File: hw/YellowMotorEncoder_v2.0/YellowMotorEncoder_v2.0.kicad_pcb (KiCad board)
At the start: 2 copper layers, 22.8 x 20.3 mm, 30 parts, among them J1 Conn_01x06, Q1 AO3401A, U1 47k, U10 10k, U11 47k, U12 18p/50V, U13 BLUE, U14 10k, U15 BLUE, U16 10k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

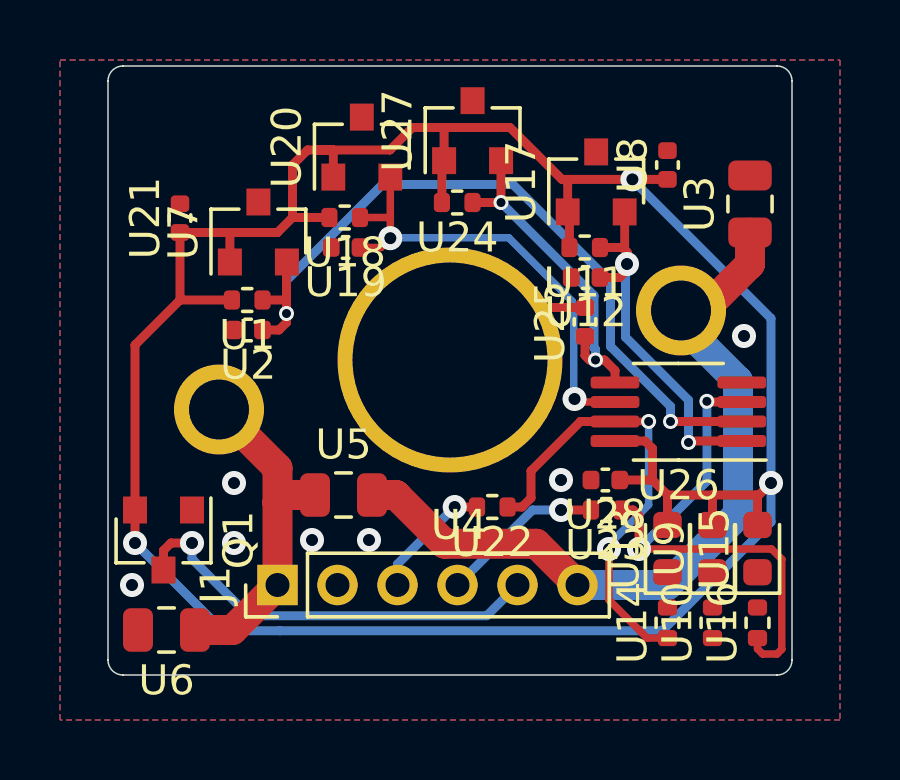
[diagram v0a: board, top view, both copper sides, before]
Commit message: 3D_viewer
i add 3d model of motor and connector
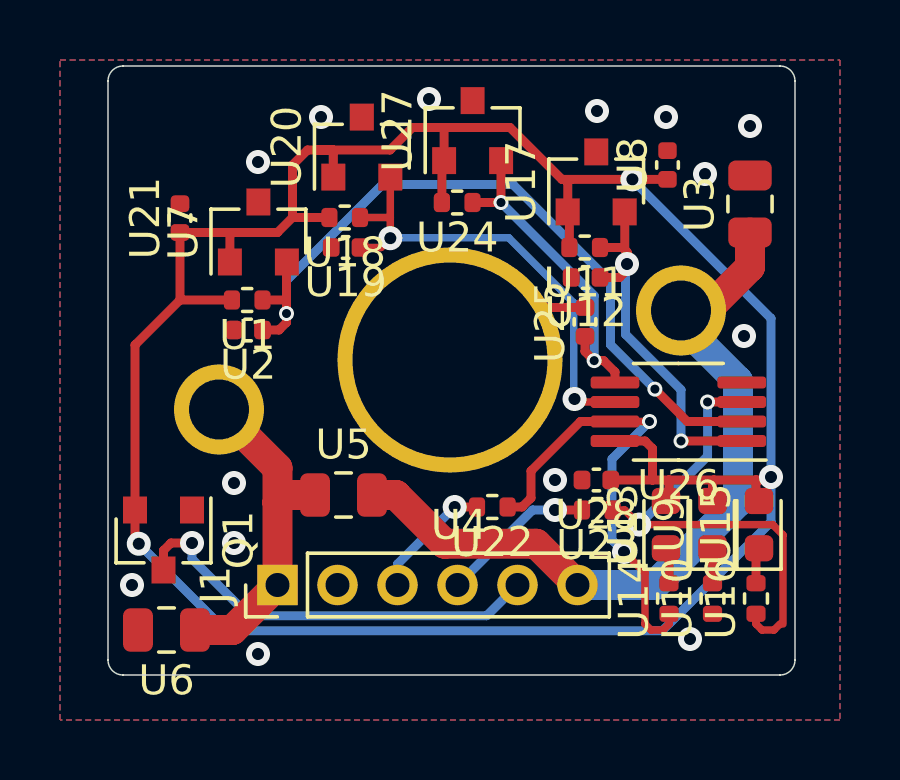
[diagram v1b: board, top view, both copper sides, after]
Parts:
- moved U14 0.81 mm to (151.3, 124.0)
- moved U16 0.81 mm to (154.2, 124.0)
- moved U10 0.81 mm to (152.8, 124.0)
- moved U13 0.80 mm to (151.2, 121.5)
- moved U15 0.80 mm to (154.3, 121.5)
- moved U9 0.80 mm to (152.8, 121.5)
- moved U23 0.30 mm to (148.9, 121.0)
- moved U28 0.30 mm to (148.9, 120.0)
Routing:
- net /~B: track 18.0 -> 16.5 mm
- net Net-(U15-Pad1): track 0.00 -> 1.12 mm
- net Net-(U13-Pad1): track 0.00 -> 1.12 mm
- net Net-(U10-Pad2): track 0.00 -> 1.12 mm
- net VCC: track 88.8 -> 87.9 mm
- net GND: vias 7 -> 14
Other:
- board size 22.8 x 20.3 mm -> 22.9 x 20.3 mm

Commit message: rotate sensors
I changing position of sensors and rotating it in circle around hole for shaft of motor.
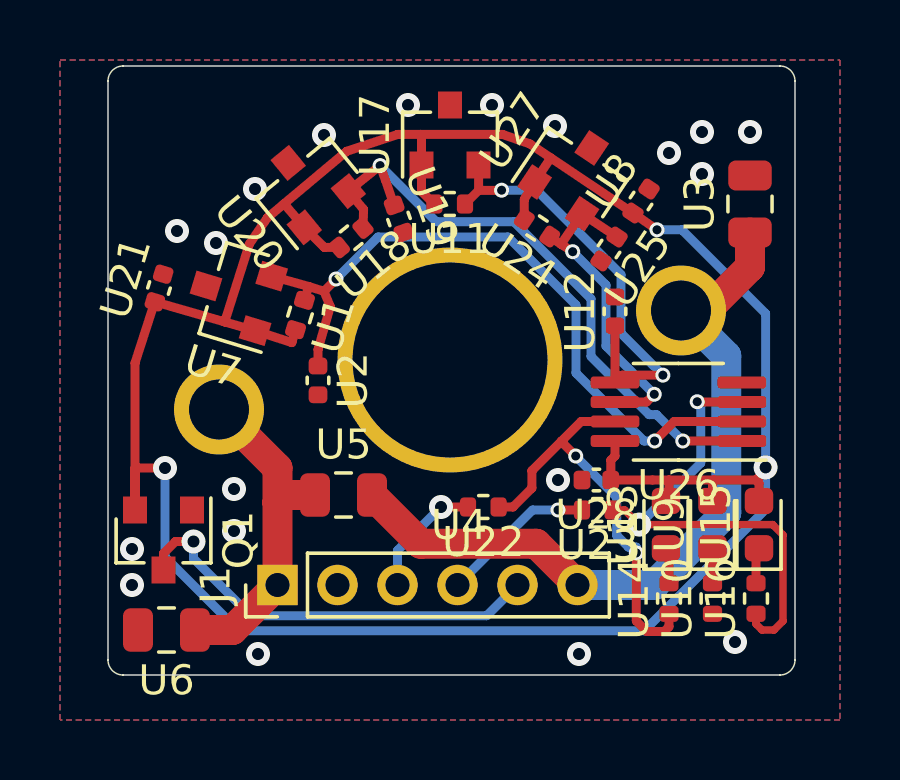
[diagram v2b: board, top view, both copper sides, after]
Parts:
- moved U17 5.12 mm to (144.0, 108.5)
- moved U11 4.73 mm to (144.0, 110.8)
- moved U27 3.69 mm to (148.2, 109.8), turned to 56.2 degrees
- moved U2 2.87 mm to (139.6, 116.7), turned to 270 degrees
- moved U24 2.79 mm to (146.9, 111.6), turned to 146.2 degrees
- moved U25 2.56 mm to (149.3, 112.3), turned to 236.2 degrees
- moved U21 2.43 mm to (134.3, 113.6), turned to 73.1 degrees
- moved U20 2.23 mm to (139.2, 110.2), turned to 129.4 degrees
- moved U7 2.23 mm to (136.8, 113.8), turned to 163.1 degrees
- moved U19 2.02 mm to (142.3, 111.3), turned to 289.7 degrees
- moved U1 1.83 mm to (139.0, 114.5), turned to 253.1 degrees
- moved U12 1.50 mm to (149.5, 114.4), turned to 90 degrees
- moved U8 1.49 mm to (150.4, 110.7), turned to 56.2 degrees
- moved U18 0.71 mm to (140.7, 111.9), turned to 219.4 degrees
- moved U22 0.30 mm to (145.1, 120.9)
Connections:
- U11 pad 1: /A1 -> /B1
- U12 pad 1: /A1 -> /B1
- U17 pad 2: /A1 -> /B1
- U18 pad 1: /B0 -> /A1
- U19 pad 1: /B0 -> /A1
- U20 pad 2: /B0 -> /A1
- U24 pad 1: /B1 -> /B0
- U25 pad 1: /B1 -> /B0
- U27 pad 2: /B1 -> /B0
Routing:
- net /A1: track 12.6 -> 21.2 mm
- net /B0: track 15.8 -> 10.8 mm
- net /B1: track 11.0 -> 14.9 mm
- net GND: track 5.22 -> 2.47 mm, vias 14 -> 19
- net /A0: track 25.8 -> 24.0 mm
- net VCC: track 87.9 -> 86.5 mm
- net /~A: track 15.5 -> 14.3 mm
